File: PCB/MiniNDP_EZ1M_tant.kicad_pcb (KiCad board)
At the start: 2 copper layers, 60 x 34 mm, 21 parts, among them J1 Conn_02x20_Odd_Even, U1 AS6C8008_TSOPII, U2 HC238, U3 4040, U4 FCT841

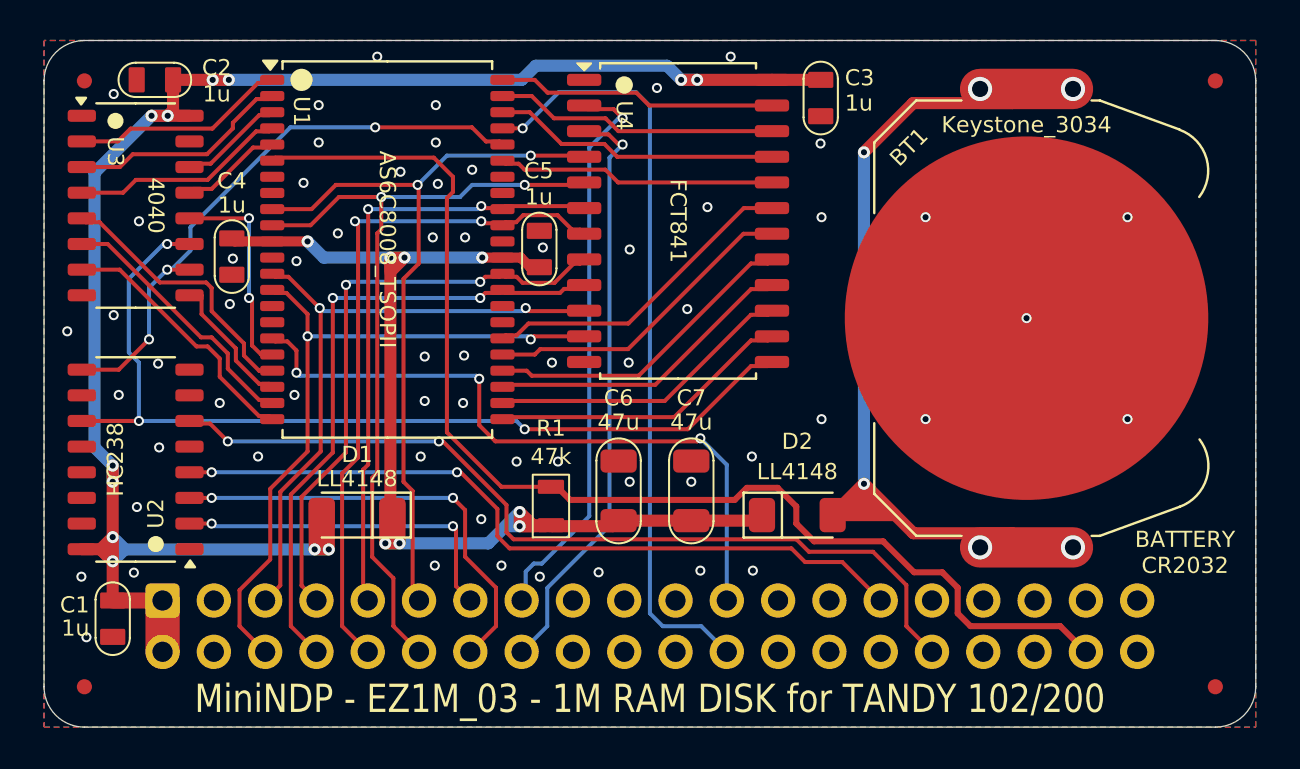
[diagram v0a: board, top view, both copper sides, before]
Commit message: make EZ1M the default
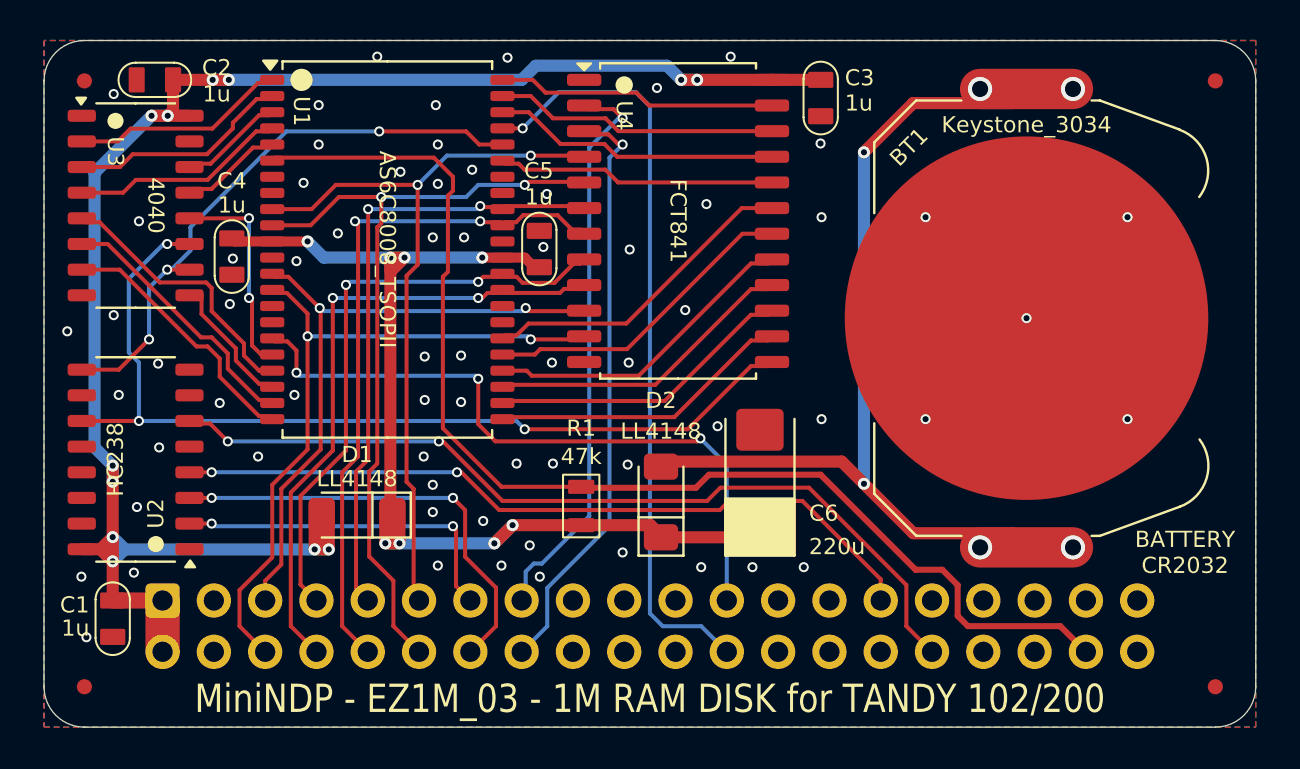
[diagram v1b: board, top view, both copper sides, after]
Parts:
- removed C7: 47u, 000_LOCAL:C_1206
- C6: value 47u -> 220u; footprint 000_LOCAL:C_1206 -> 000_LOCAL:CP_6032
- moved C6 7.02 mm to (157.4, 107.8)
- moved D2 6.78 mm to (152.5, 108.9), turned to 90 degrees
- moved R1 1.50 mm to (148.6, 109.1)
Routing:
- net +BATT: track 37.3 -> 45.7 mm
- net GND: vias 62 -> 67

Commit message: re-add inrush resistor to EZ1M_tant
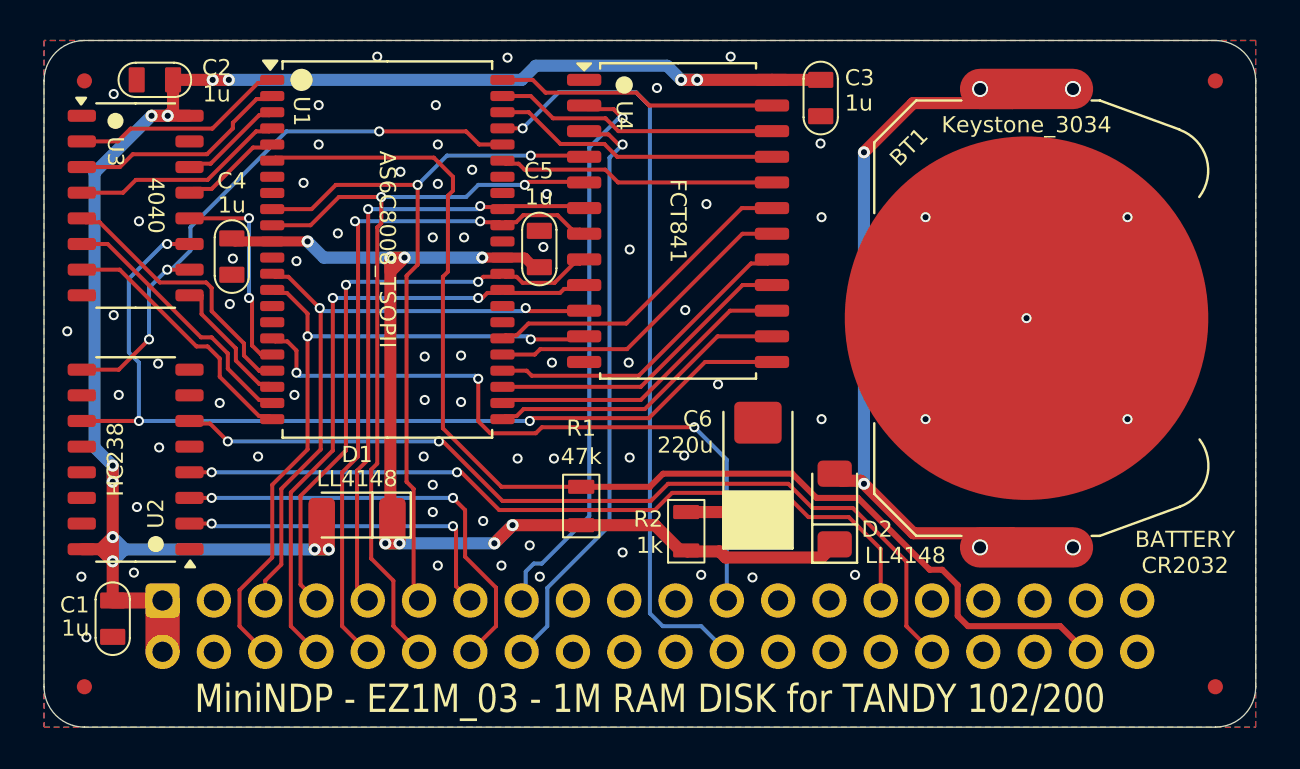
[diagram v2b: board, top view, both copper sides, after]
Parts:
- added R2: 1k, 000_LOCAL:R_0805, F.Cu at (153.8, 110.3)
- moved D2 8.61 mm to (161.1, 109.2)
- moved C6 0.36 mm to (157.3, 107.4)
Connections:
- C6 pad 1: VMEM -> Net-(C6-Pad1)
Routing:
- net +BATT: track 45.7 -> 36.8 mm
- net VMEM: track 49.2 -> 53.4 mm
- net Net-(C6-Pad1): track 0.00 -> 3.76 mm
- net /~{Y0}: track 37.8 -> 39.1 mm
- net /(A): track 43.2 -> 44.1 mm
- net GND: vias 67 -> 68
